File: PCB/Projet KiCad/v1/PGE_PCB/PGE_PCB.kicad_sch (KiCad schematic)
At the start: 1 part, among them U1 STM32L476RGTx

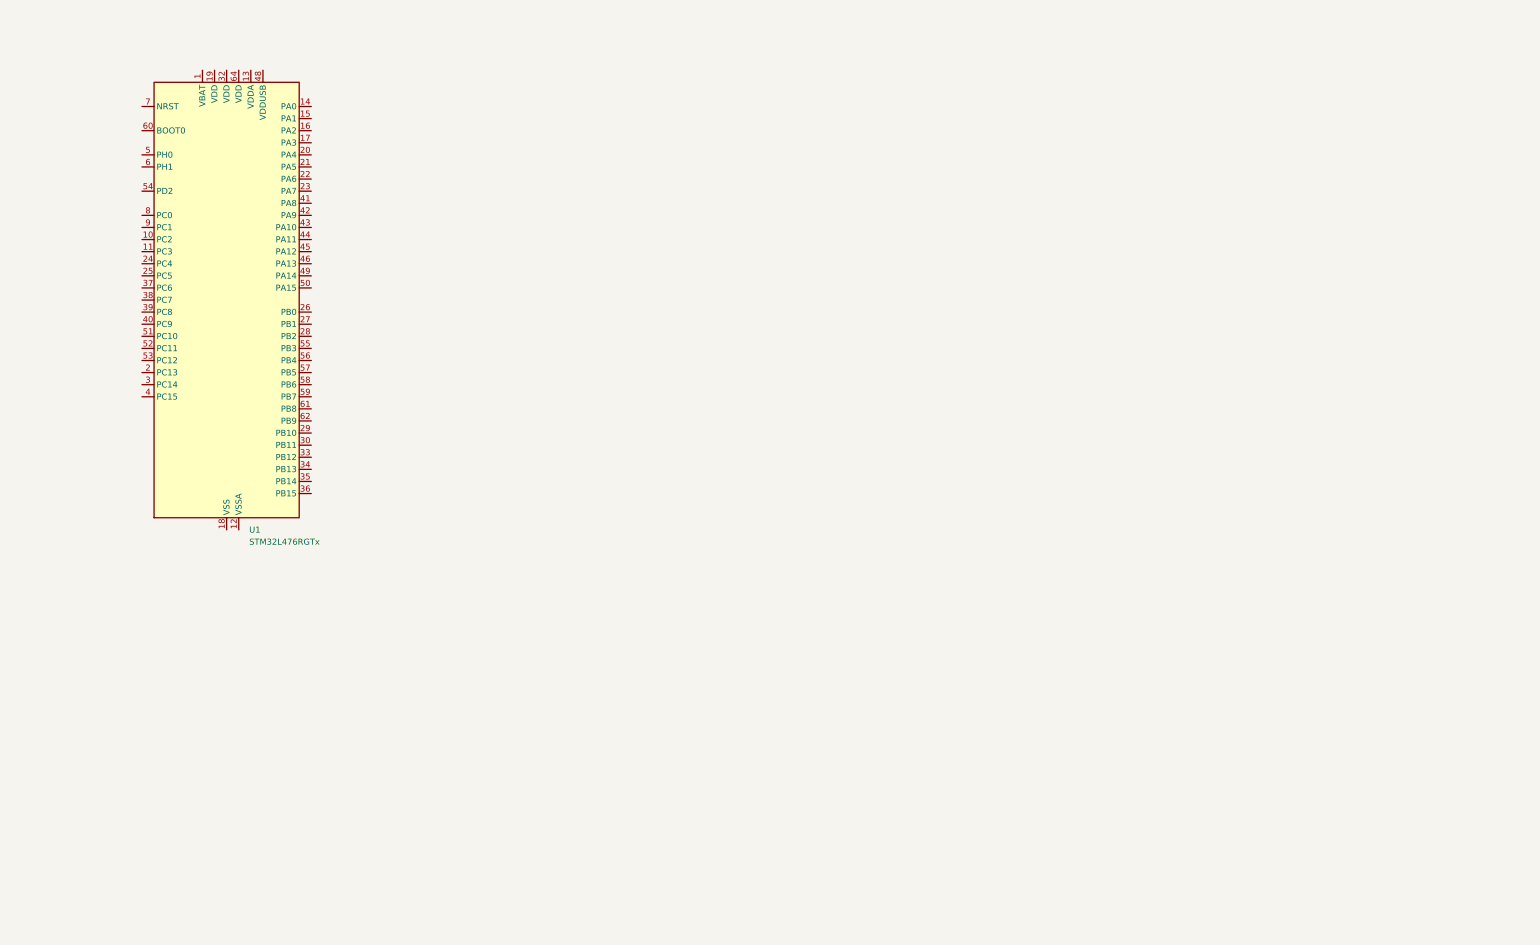
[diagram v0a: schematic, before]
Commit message: Modification Schéma PCB (19/12) -Ajout Module alimentation -Ajout Module GPS -Ajout Port USB Kristen
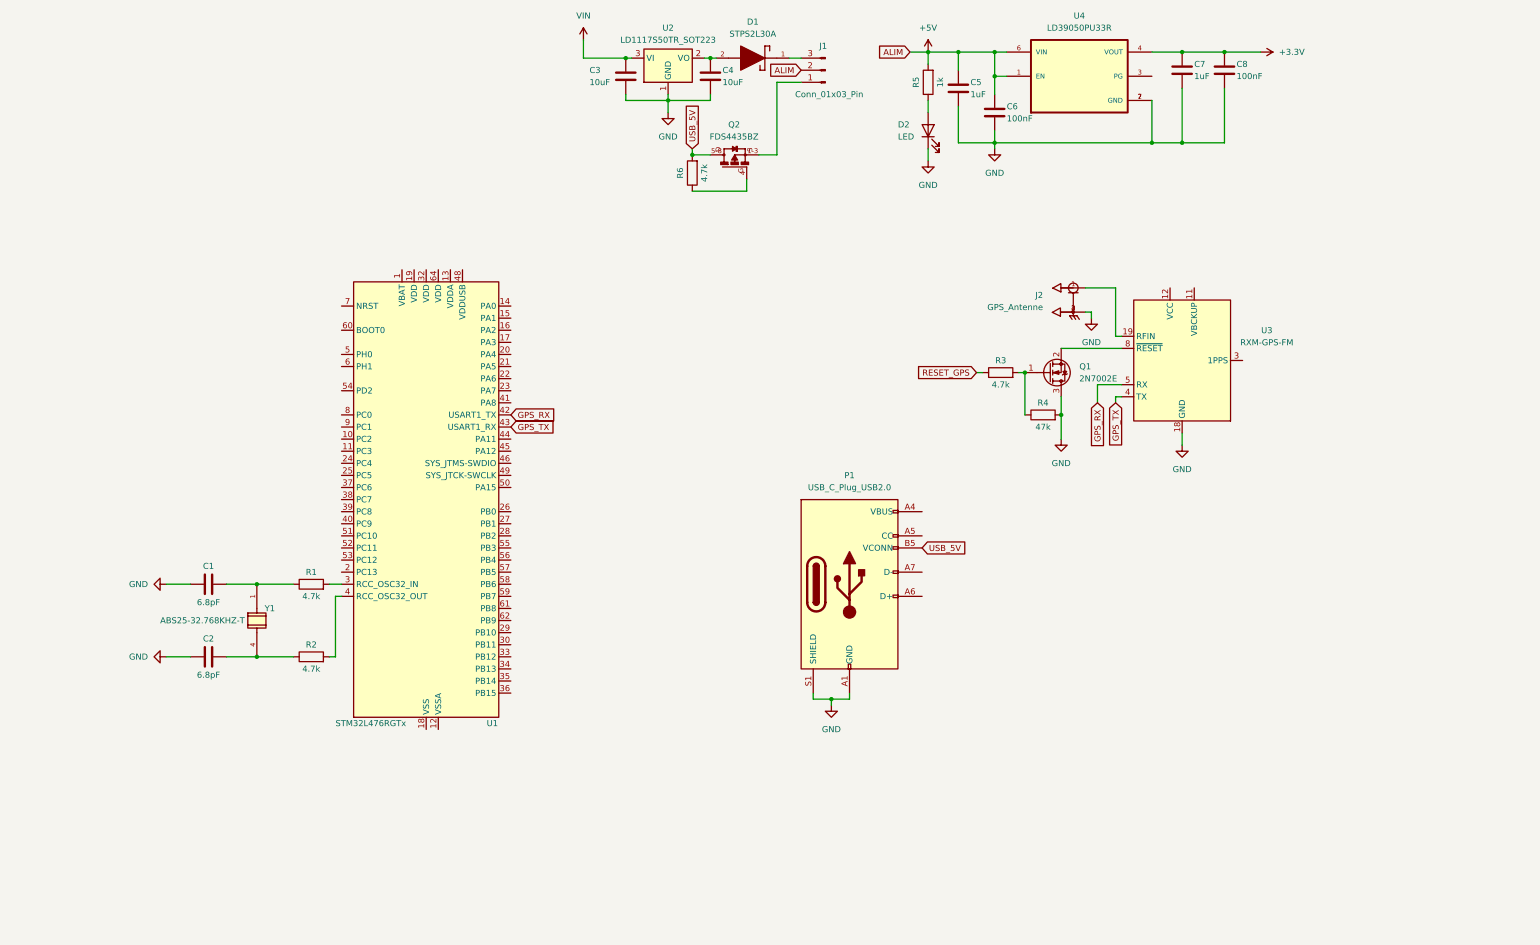
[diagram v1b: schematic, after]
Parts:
- added C1, C2: 6.8pF, Capacitor_SMD:C_0603_1608Metric, symbol Device:C
- added C3, C4: 10uF, Capacitor_SMD:C_0603_1608Metric, symbol Device:C
- added C5, C7: 1uF, Capacitor_SMD:C_0603_1608Metric, symbol Device:C
- added C6, C8: 100nF, Capacitor_SMD:C_0603_1608Metric, symbol Device:C
- added D1: STPS2L30A, STPS2L30A:DIOM5126X265N, symbol STPS2L30A:STPS2L30A
- added D2: LED, LED_SMD:LED_0805_2012Metric, symbol Device:LED
- added J1: Conn_01x03_Pin, Connector_PinHeader_2.54mm:PinHeader_1x03_P2.54mm_Vertical, symbol Connector:Conn_01x03_Pin
- added J2: GPS_Antenne, 20449-001E-03:IPEX_20449-001E-03, symbol 20449-001E-03:20449-001E-03
- added P1: USB_C_Plug_USB2.0, Connector_USB:USB_C_Plug_Molex_105444, symbol Connector:USB_C_Plug_USB2.0
- added Q1: 2N7002E, Package_TO_SOT_SMD:SOT-23, symbol Transistor_FET:2N7002E
- added Q2: FDS4435BZ, FDS4435BZ:SO08-E3, symbol FDS4435BZ:FDS4435BZ
- added R1, R2: 4.7k, Capacitor_SMD:C_0201_0603Metric, symbol Device:R
- added R3, R6: 4.7k, Resistor_SMD:R_0603_1608Metric, symbol Device:R
- added R4: 47k, Resistor_SMD:R_0603_1608Metric, symbol Device:R
- added R5: 1k, Resistor_SMD:R_0603_1608Metric, symbol Device:R
- added U2: LD1117S50TR_SOT223, Package_TO_SOT_SMD:SOT-223-3_TabPin2, symbol Regulator_Linear:LD1117S50TR_SOT223
- added U3: RXM-GPS-FM, RF_GPS:Linx_RXM-GPS, symbol RF_GPS:RXM-GPS-FM
- added U4: LD39050PU33R, LD39050PU33R:SON95P300X300X100-7N, symbol LD39050PU33R:LD39050PU33R
- added Y1: ABS25-32.768KHZ-T, ABS25-32.768KHZ-T:XTAL_ABS25-32.768KHZ-6-1-T, symbol ABS25-32.768KHZ-T:ABS25-32.768KHZ-T
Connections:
- net at U1.3 (PC14): now also R1.2
- net at U1.4 (PC15): now also R2.2
- net GPS_RX: now reaches U1.42 (PA9)
- net GPS_RX: now also U3.5 (RX)
- net GPS_TX: now reaches U1.43 (PA10)
- net GPS_TX: now also U3.4 (TX)
- new net: C1.2, R1.1, Y1.1
- new net: C2.2, R2.1, Y1.4
- new net: J2.1, U3.19 (RFIN)
- new net: Q1.2 (S), U3.8 (~{RESET})
- new net: P1.A4 (VBUS), P1.A9 (VBUS), P1.B4 (VBUS), P1.B9 (VBUS)
- new net: J1.1 (Pin_1), Q2.1-3
- new net: Q2.4, R6.1
- new net: C4.1, D1.2, U2.2 (VO)
- new net: D2.2 (A), R5.1
- new net: Q1.1 (G), R3.2, R4.1
- new net: D1.1, J1.3 (Pin_3)
- new net +3.3V: C7.1, C8.1, U4.4 (VOUT)
- new net +5V: C5.1, C6.1, J1.2 (Pin_2), R5.2, U4.1 (EN), U4.6 (VIN)
- new net GND: C1.1, C2.1, C3.2, C4.2, C5.2, C6.2, C7.2, C8.2, D2.1 (K), J2.2, J2.3, J2.4, P1.A1 (GND), P1.A12 (GND), P1.B1 (GND), P1.B12 (GND), P1.S1 (SHIELD), Q1.3 (D), R4.2, U2.1 (GND), U3.18 (GND), U3.20 (GND), U3.21 (GND), U3.22 (GND), U4.2 (GND), U4.7 (GND)
- new net RESET_GPS: R3.1
- new net USB_5V: P1.B5 (VCONN), Q2.5-8, R6.2
- new net VIN: C3.1, U2.3 (VI)
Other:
- moved on the sheet: U1

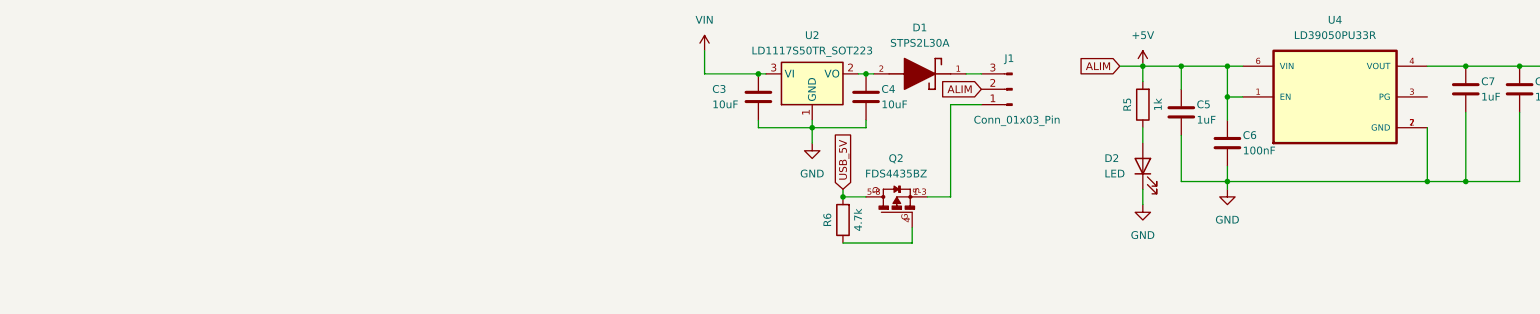
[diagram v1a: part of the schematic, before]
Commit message: Ajout sous-feuille Alimentation
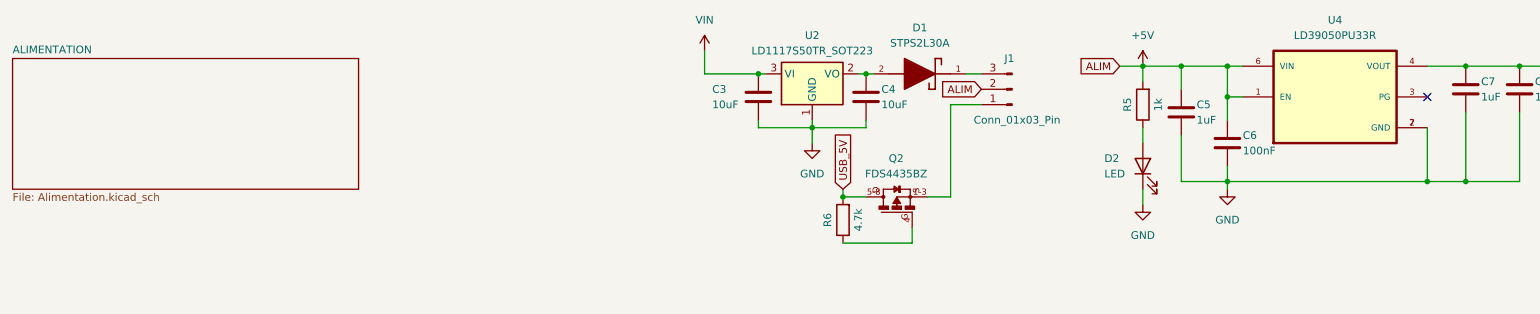
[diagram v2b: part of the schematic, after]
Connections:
- no-connect marks 0 -> 1
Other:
- added sheet ALIMENTATION (Alimentation.kicad_sch)
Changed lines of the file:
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@@
 		(color 0 0 0 0)
 	)
+	(no_connect
+		(at 251.46 26.67)
+	)
 	(wire
 		(pts
@@
 		)
 		(instances
-			(project ""
+			(project "PGE_PCB"
 				(path "/503a3176-3dc5-409a-9acd-b4c6a6fcf256"
 					(reference "Y1")
@@
 		)
 		(instances
-			(project ""
+			(project "PGE_PCB"
 				(path "/503a3176-3dc5-409a-9acd-b4c6a6fcf256"
 					(reference "#PWR011")
@@
 		)
 		(instances
-			(project ""
+			(project "PGE_PCB"
 				(path "/503a3176-3dc5-409a-9acd-b4c6a6fcf256"
 					(reference "U1")
@@
 		)
 		(instances
-			(project ""
+			(project "PGE_PCB"
 				(path "/503a3176-3dc5-409a-9acd-b4c6a6fcf256"
 					(reference "U3")
@@
 		)
 		(instances
-			(project ""
+			(project "PGE_PCB"
 				(path "/503a3176-3dc5-409a-9acd-b4c6a6fcf256"
 					(reference "P1")
@@
 		)
 		(instances
-			(project ""
+			(project "PGE_PCB"
 				(path "/503a3176-3dc5-409a-9acd-b4c6a6fcf256"
 					(reference "C3")
@@
 		)
 		(instances
-			(project ""
+			(project "PGE_PCB"
 				(path "/503a3176-3dc5-409a-9acd-b4c6a6fcf256"
 					(reference "Q2")
@@
 		)
 		(instances
-			(project ""
+			(project "PGE_PCB"
 				(path "/503a3176-3dc5-409a-9acd-b4c6a6fcf256"
 					(reference "#PWR08")
@@
 		)
 		(instances
-			(project ""
+			(project "PGE_PCB"
 				(path "/503a3176-3dc5-409a-9acd-b4c6a6fcf256"
 					(reference "C1")
@@
 		)
 		(instances
-			(project ""
+			(project "PGE_PCB"
 				(path "/503a3176-3dc5-409a-9acd-b4c6a6fcf256"
 					(reference "R1")
@@
 		)
 		(instances
-			(project ""
+			(project "PGE_PCB"
 				(path "/503a3176-3dc5-409a-9acd-b4c6a6fcf256"
 					(reference "#PWR03")
@@
 		)
 		(instances
-			(project ""
+			(project "PGE_PCB"
 				(path "/503a3176-3dc5-409a-9acd-b4c6a6fcf256"
 					(reference "Q1")
@@
 		)
 		(instances
-			(project ""
+			(project "PGE_PCB"
 				(path "/503a3176-3dc5-409a-9acd-b4c6a6fcf256"
 					(reference "D2")
@@
 		)
 		(instances
-			(project ""
+			(project "PGE_PCB"
 				(path "/503a3176-3dc5-409a-9acd-b4c6a6fcf256"
 					(reference "#PWR07")
@@
 		)
 		(instances
-			(project ""
+			(project "PGE_PCB"
 				(path "/503a3176-3dc5-409a-9acd-b4c6a6fcf256"
 					(reference "#PWR012")
@@
 		)
 		(instances
-			(project ""
+			(project "PGE_PCB"
 				(path "/503a3176-3dc5-409a-9acd-b4c6a6fcf256"
 					(reference "U2")
@@
 		)
 		(instances
-			(project ""
+			(project "PGE_PCB"
 				(path "/503a3176-3dc5-409a-9acd-b4c6a6fcf256"
 					(reference "#PWR010")
@@
 		)
 		(instances
-			(project ""
+			(project "PGE_PCB"
 				(path "/503a3176-3dc5-409a-9acd-b4c6a6fcf256"
 					(reference "#PWR01")
@@
 		)
 		(instances
-			(project ""
+			(project "PGE_PCB"
 				(path "/503a3176-3dc5-409a-9acd-b4c6a6fcf256"
 					(reference "#PWR04")
@@
 		)
 		(instances
-			(project ""
+			(project "PGE_PCB"
 				(path "/503a3176-3dc5-409a-9acd-b4c6a6fcf256"
 					(reference "#PWR06")
@@
 		)
 		(instances
-			(project ""
+			(project "PGE_PCB"
 				(path "/503a3176-3dc5-409a-9acd-b4c6a6fcf256"
 					(reference "R3")
@@
 		)
 		(instances
-			(project ""
+			(project "PGE_PCB"
 				(path "/503a3176-3dc5-409a-9acd-b4c6a6fcf256"
 					(reference "J2")
@@
 		)
 		(instances
-			(project ""
+			(project "PGE_PCB"
 				(path "/503a3176-3dc5-409a-9acd-b4c6a6fcf256"
 					(reference "U4")
@@
 		)
 		(instances
-			(project ""
+			(project "PGE_PCB"
 				(path "/503a3176-3dc5-409a-9acd-b4c6a6fcf256"
 					(reference "J1")
@@
 		)
 		(instances
-			(project ""
+			(project "PGE_PCB"
 				(path "/503a3176-3dc5-409a-9acd-b4c6a6fcf256"
 					(reference "D1")
@@
 		)
 		(instances
-			(project ""
+			(project "PGE_PCB"
 				(path "/503a3176-3dc5-409a-9acd-b4c6a6fcf256"
 					(reference "#PWR05")
@@
 		)
 		(instances
-			(project ""
+			(project "PGE_PCB"
 				(path "/503a3176-3dc5-409a-9acd-b4c6a6fcf256"
 					(reference "#PWR09")
@@
 				)
 			)
+		)
+	)
+	(sheet
+		(at 17.78 20.32)
+		(size 57.15 21.59)
+		(fields_autoplaced yes)
+		(stroke
+			(width 0.1524)
+			(type solid)
+		)
+		(fill
+			(color 0 0 0 0.0000)
+		)
+		(property "Sheetname" "ALIMENTATION"
+			(at 17.78 19.6084 0)
+			(effects
+				(font
+					(size 1.27 1.27)
+				)
+				(justify left bottom)
+			)
+		)
+		(property "Sheetfile" "Alimentation.kicad_sch"
+			(at 17.78 42.4946 0)
+			(effects
+				(font
+					(size 1.27 1.27)
+				)
+				(justify left top)
+			)
+		)
+		(instances
+			(project "PGE_PCB"
+				(path "/503a3176-3dc5-409a-9acd-b4c6a6fcf256"
+					(page "2")
+				)
+			)

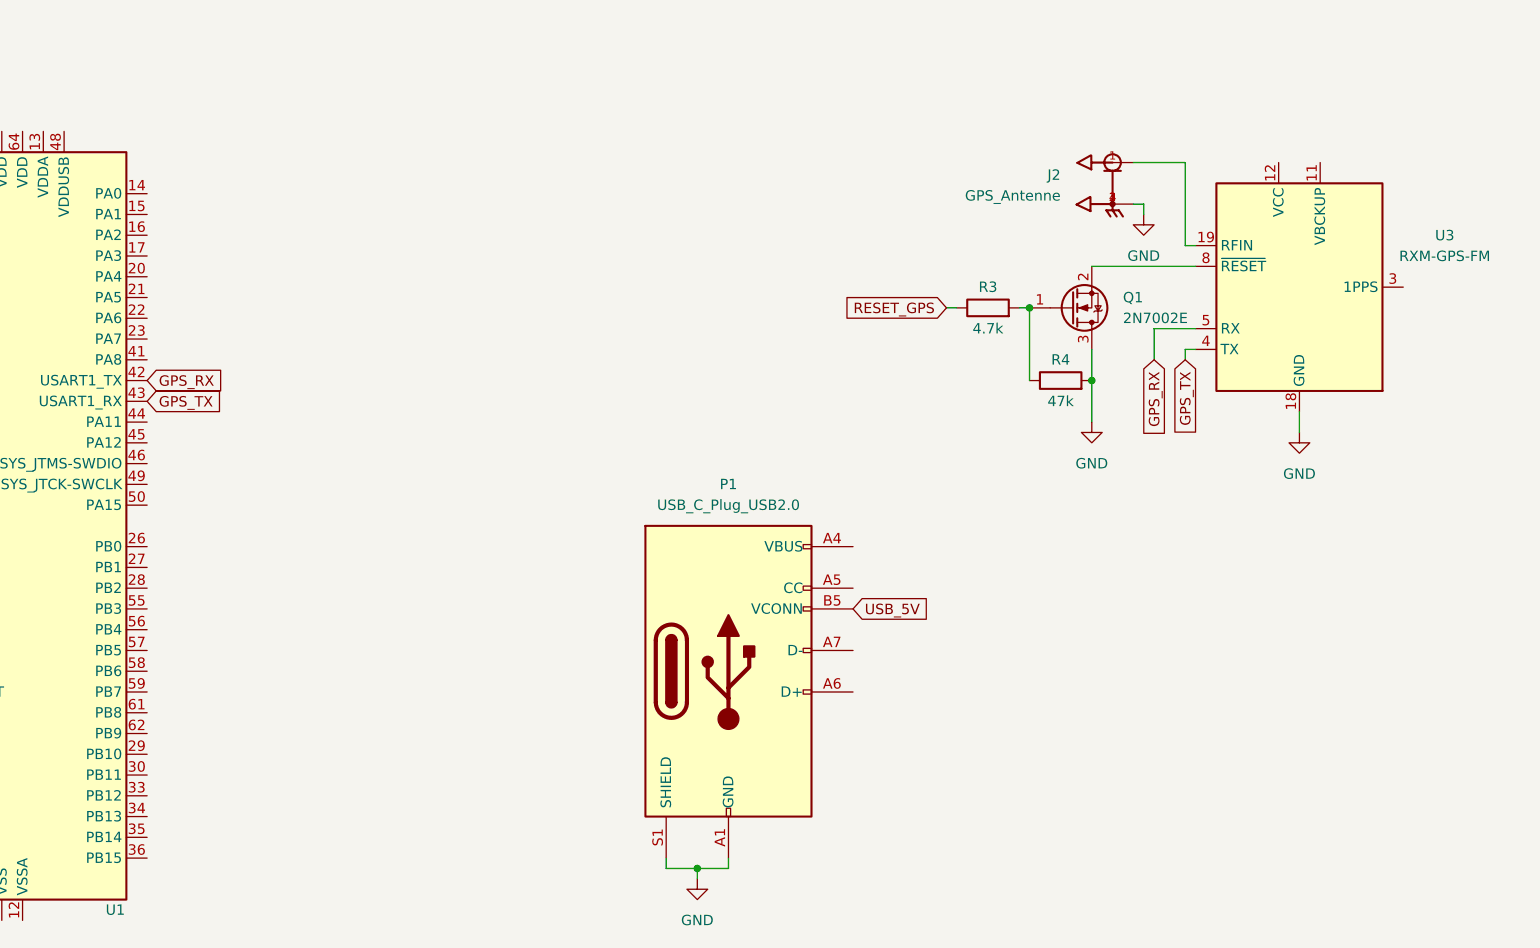
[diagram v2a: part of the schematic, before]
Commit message: Maj PCB
- correction module GPS (I2C)
- ajout module LoRa RFM9x
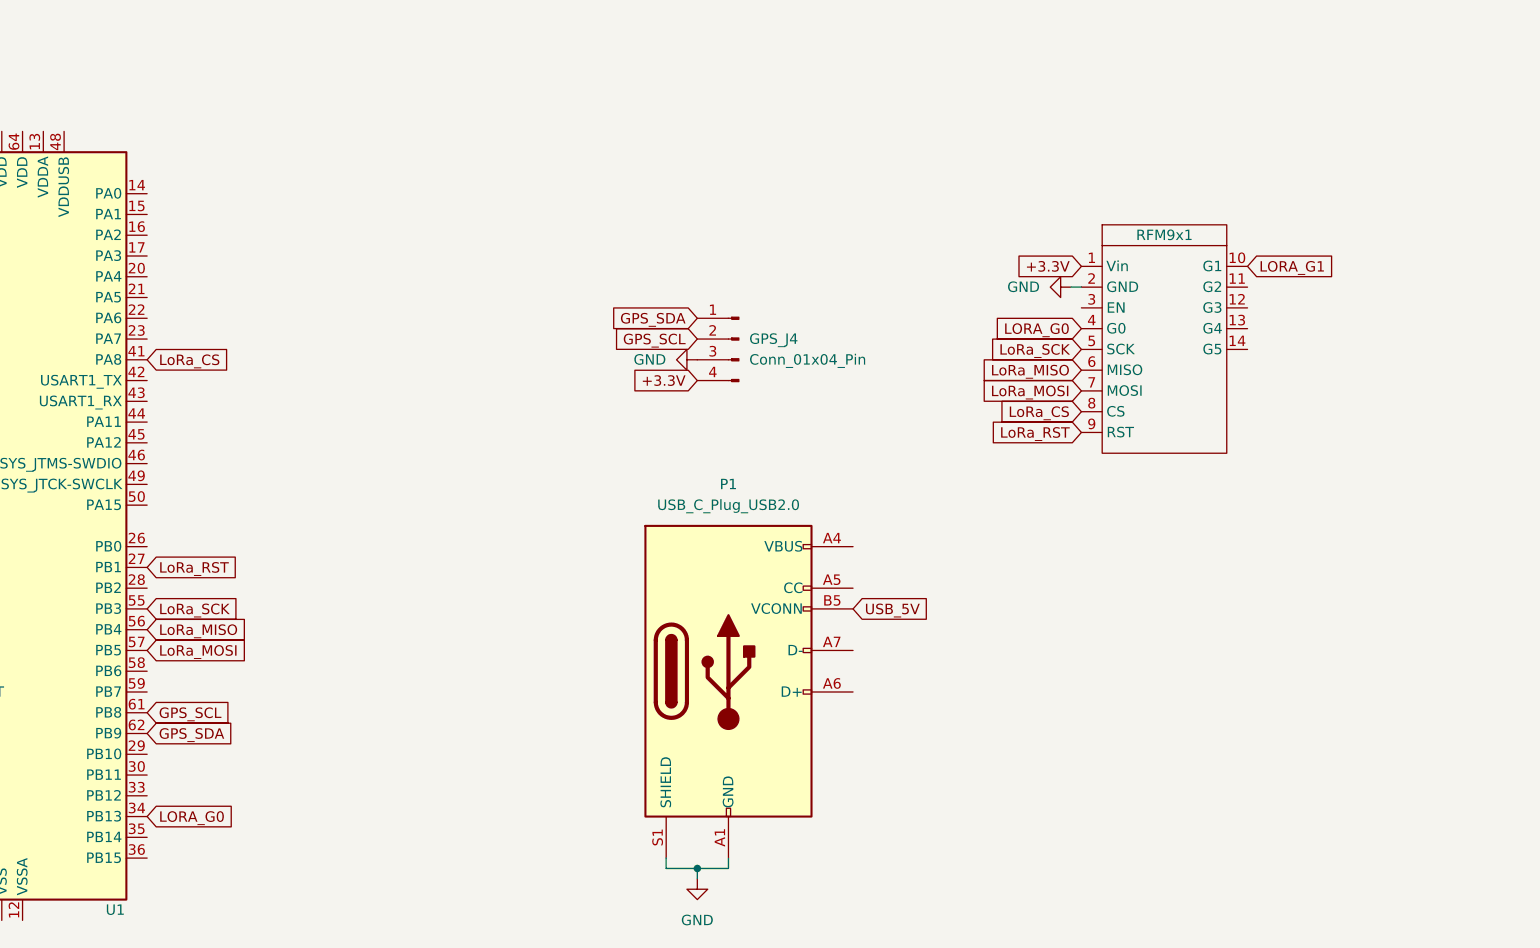
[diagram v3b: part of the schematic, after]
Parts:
- removed J2: GPS_Antenne, 20449-001E-03:IPEX_20449-001E-03, symbol 20449-001E-03:20449-001E-03
- removed Q1: 2N7002E, Package_TO_SOT_SMD:SOT-23, symbol Transistor_FET:2N7002E
- removed R3: 4.7k, Resistor_SMD:R_0603_1608Metric, symbol Device:R
- removed R4: 47k, Resistor_SMD:R_0603_1608Metric, symbol Device:R
- removed U3: RXM-GPS-FM, RF_GPS:Linx_RXM-GPS, symbol RF_GPS:RXM-GPS-FM
- added GPS_J4: Conn_01x04_Pin, Connector_PinHeader_1.00mm:PinHeader_1x04_P1.00mm_Vertical, symbol Connector:Conn_01x04_Pin
- added RFM9x1: ~, LoRa_Breakout:LoRa_Breakout, symbol LoRa_Breakout:RFM9x
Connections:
- net +3.3V: now also GPS_J4.4 (Pin_4), RFM9x1.1 (Vin)
- net GND: now also GPS_J4.3 (Pin_3), RFM9x1.2 (GND)
- net LoRa_RST: now reaches U1.27 (PB1)
- net LoRa_RST: now also RFM9x1.9 (RST)
- net LORA_G0: now reaches U1.34 (PB13)
- net LORA_G0: now also RFM9x1.4 (G0)
- net LoRa_CS: now reaches U1.41 (PA8)
- net LoRa_CS: now also RFM9x1.8 (CS)
- net LoRa_SCK: now reaches U1.55 (PB3)
- net LoRa_SCK: now also RFM9x1.5 (SCK)
- net LoRa_MISO: now reaches U1.56 (PB4)
- net LoRa_MISO: now also RFM9x1.6 (MISO)
- net LoRa_MOSI: now reaches U1.57 (PB5)
- net LoRa_MOSI: now also RFM9x1.7 (MOSI)
- net GPS_SCL: now reaches U1.61 (PB8)
- net GPS_SCL: now also GPS_J4.2 (Pin_2)
- net GPS_SDA: now reaches U1.62 (PB9)
- net GPS_SDA: now also GPS_J4.1 (Pin_1)
- net GPS_RX: no longer names the net of U1.42 (PA9)
- net GPS_TX: no longer names the net of U1.43 (PA10)
- new net LORA_G1: RFM9x1.10 (G1)
